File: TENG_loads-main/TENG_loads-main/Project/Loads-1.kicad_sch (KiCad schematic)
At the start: 24 parts, among them K1 V23079C1103B301, K10 IMC03TS, K11 V23079C1103B301, K12 V23079C1103B301, K13 V23079C1103B301, K14 IMC03TS, K15 IMC03TS, K16 IMC03TS, K2 V23079C1103B301, K3 V23079C1103B301, K4 V23079C1103B301, K5 V23079C1103B301, K6 IMC03TS, K7 IMC03TS, K8 IMC03TS, K9 IMC03TS

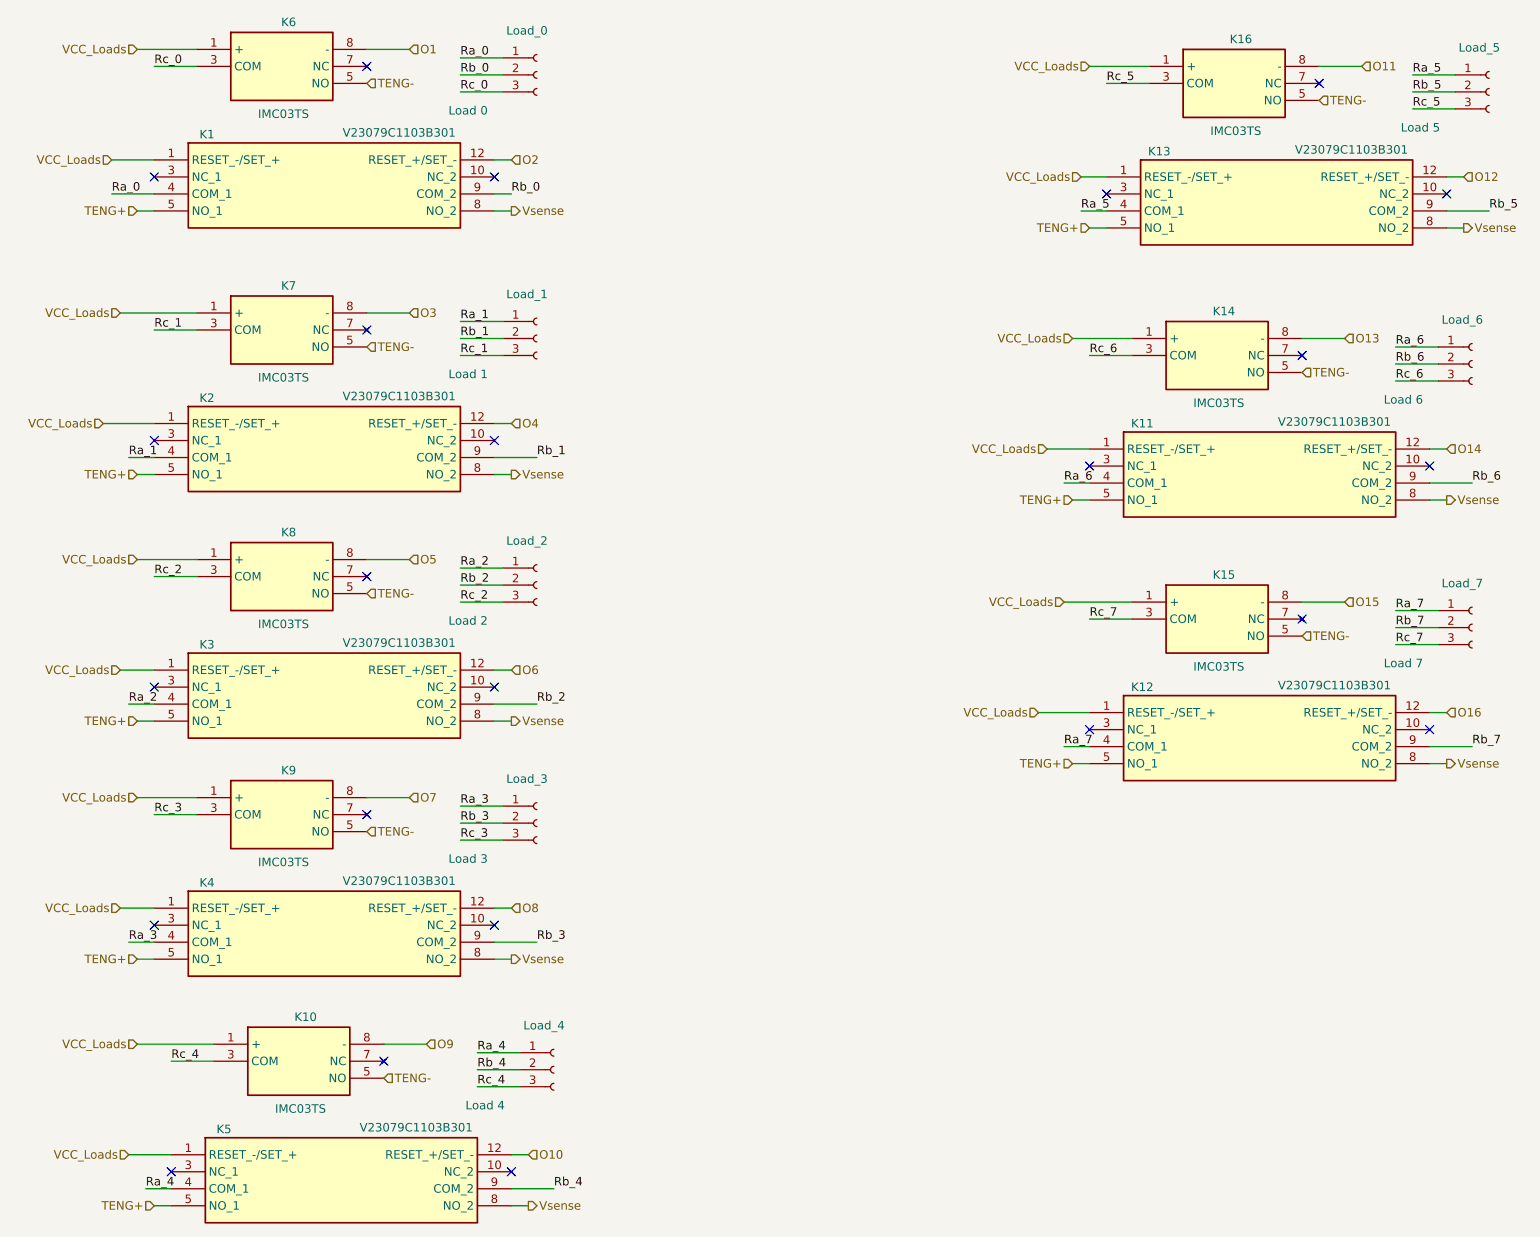
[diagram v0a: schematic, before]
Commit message: Changed Relay identifier
Changed relay identifier with the correct one (12 VDC changed to 5 VDC).
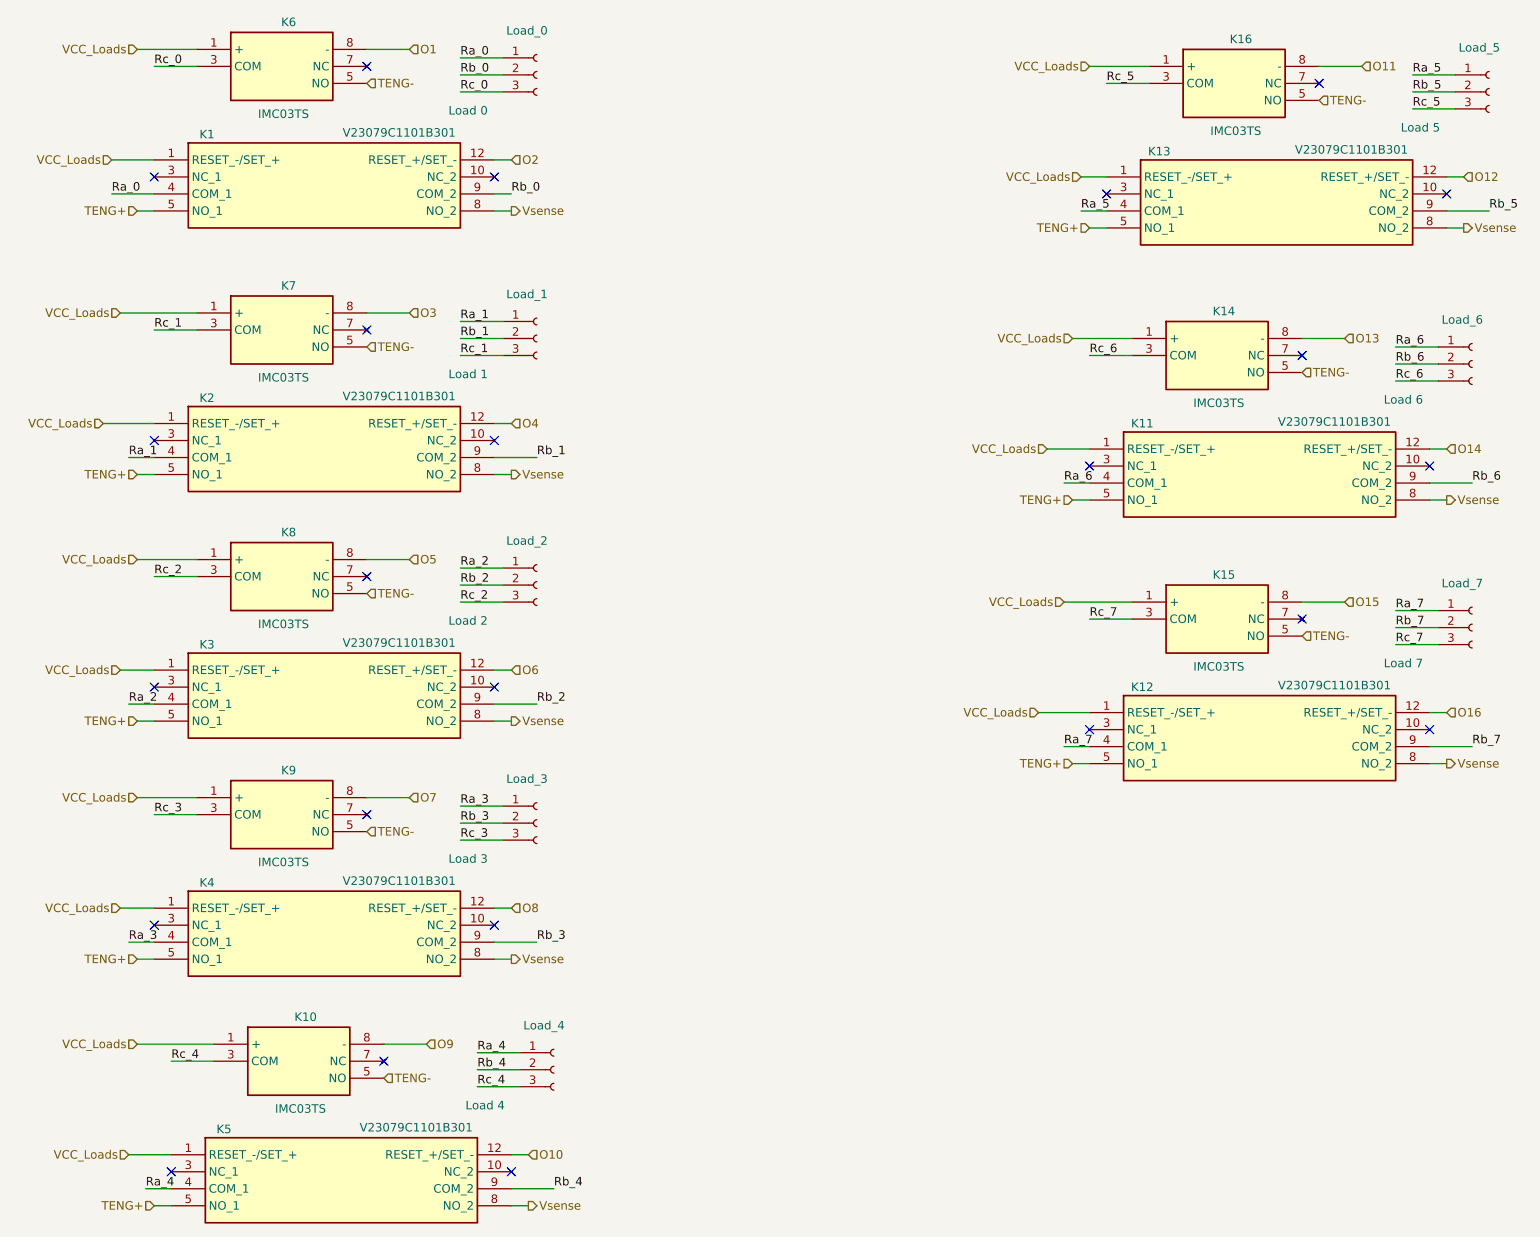
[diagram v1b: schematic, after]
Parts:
- K1, K11, K12, K13, K2, K3, K4, K5: value V23079C1103B301 -> V23079C1101B301
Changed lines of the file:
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@@
 			)
 		)
-		(property "Value" "V23079C1103B301"
+		(property "Value" "V23079C1101B301"
 			(at 105.156 72.136 0)
 			(effects
@@
 			)
 		)
-		(property "Value" "V23079C1103B301"
+		(property "Value" "V23079C1101B301"
 			(at 107.696 181.356 0)
 			(effects
@@
 			)
 		)
-		(property "Value" "V23079C1103B301"
+		(property "Value" "V23079C1101B301"
 			(at 244.856 115.316 0)
 			(effects
@@
 			)
 		)
-		(property "Value" "V23079C1103B301"
+		(property "Value" "V23079C1101B301"
 			(at 105.156 144.526 0)
 			(effects
@@
 			)
 		)
-		(property "Value" "V23079C1103B301"
+		(property "Value" "V23079C1101B301"
 			(at 247.396 35.306 0)
 			(effects
@@
 			)
 		)
-		(property "Value" "V23079C1103B301"
+		(property "Value" "V23079C1101B301"
 			(at 244.856 75.946 0)
 			(effects
@@
 			)
 		)
-		(property "Value" "V23079C1103B301"
+		(property "Value" "V23079C1101B301"
 			(at 105.156 108.966 0)
 			(effects
@@
 			)
 		)
-		(property "Value" "V23079C1103B301"
+		(property "Value" "V23079C1101B301"
 			(at 105.156 32.766 0)
 			(effects

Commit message: Capacitor and relay changes
Capacitor correction and relay ID correction
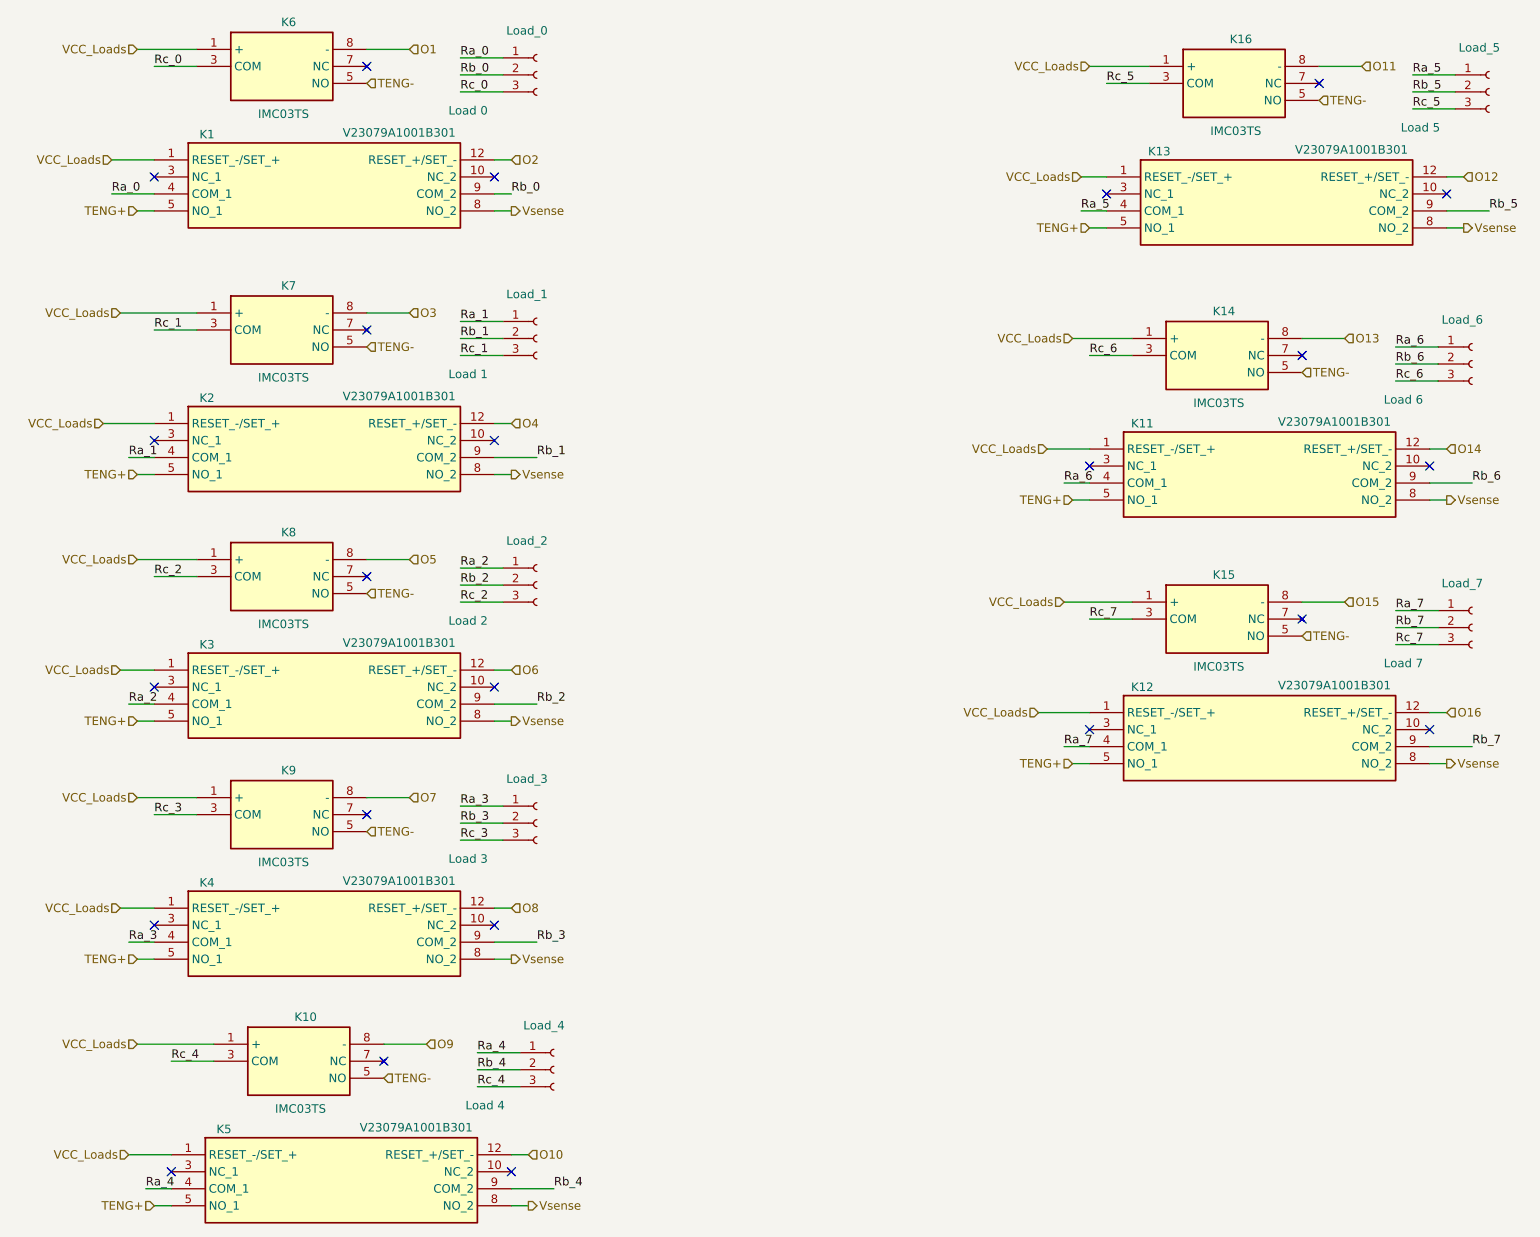
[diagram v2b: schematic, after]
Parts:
- K1, K11, K12, K13, K2, K3, K4, K5: value V23079C1101B301 -> V23079A1001B301
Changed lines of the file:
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@@
 			)
 		)
-		(property "Value" "V23079C1101B301"
+		(property "Value" "V23079A1001B301"
 			(at 105.156 72.136 0)
 			(effects
@@
 			)
 		)
-		(property "Value" "V23079C1101B301"
+		(property "Value" "V23079A1001B301"
 			(at 107.696 181.356 0)
 			(effects
@@
 			)
 		)
-		(property "Value" "V23079C1101B301"
+		(property "Value" "V23079A1001B301"
 			(at 244.856 115.316 0)
 			(effects
@@
 			)
 		)
-		(property "Value" "V23079C1101B301"
+		(property "Value" "V23079A1001B301"
 			(at 105.156 144.526 0)
 			(effects
@@
 			)
 		)
-		(property "Value" "V23079C1101B301"
+		(property "Value" "V23079A1001B301"
 			(at 247.396 35.306 0)
 			(effects
@@
 			)
 		)
-		(property "Value" "V23079C1101B301"
+		(property "Value" "V23079A1001B301"
 			(at 244.856 75.946 0)
 			(effects
@@
 			)
 		)
-		(property "Value" "V23079C1101B301"
+		(property "Value" "V23079A1001B301"
 			(at 105.156 108.966 0)
 			(effects
@@
 			)
 		)
-		(property "Value" "V23079C1101B301"
+		(property "Value" "V23079A1001B301"
 			(at 105.156 32.766 0)
 			(effects
